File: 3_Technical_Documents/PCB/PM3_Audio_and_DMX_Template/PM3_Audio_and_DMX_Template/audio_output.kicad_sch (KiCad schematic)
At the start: 34 parts, among them U12 OPA2134

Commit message: new push
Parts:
- removed C52: 2.2nF COG, Capacitor_SMD:C_0603_1608Metric, symbol Device:C
- removed C61: 22u, Capacitor_SMD:CP_Elec_6.3x7.7, symbol Device:C_Polarized
- removed R65: 4.99k, Resistor_SMD:R_0603_1608Metric, symbol Device:R
- renumbered C50 to C66, C57 to C67, C54 to C68, C58 to C69, C55 to C71, C59 to C72, C56 to C73, C60 to C74, C47 to C75, C51 to C76, C62 to C77, C49 to C78, C53 to C79, C72 to C80, R24 to R46, R37 to R47, R39 to R48, R40 to R49, R38 to R50, R41 to R51, R31 to R52, R36 to R53, R42 to R54, R43 to R55, R32 to R56, R44 to R57, R34 to R58, R45 to R59, R35 to R60, R46 to R61, U12 to U14
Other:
- note added: "Analog Output"

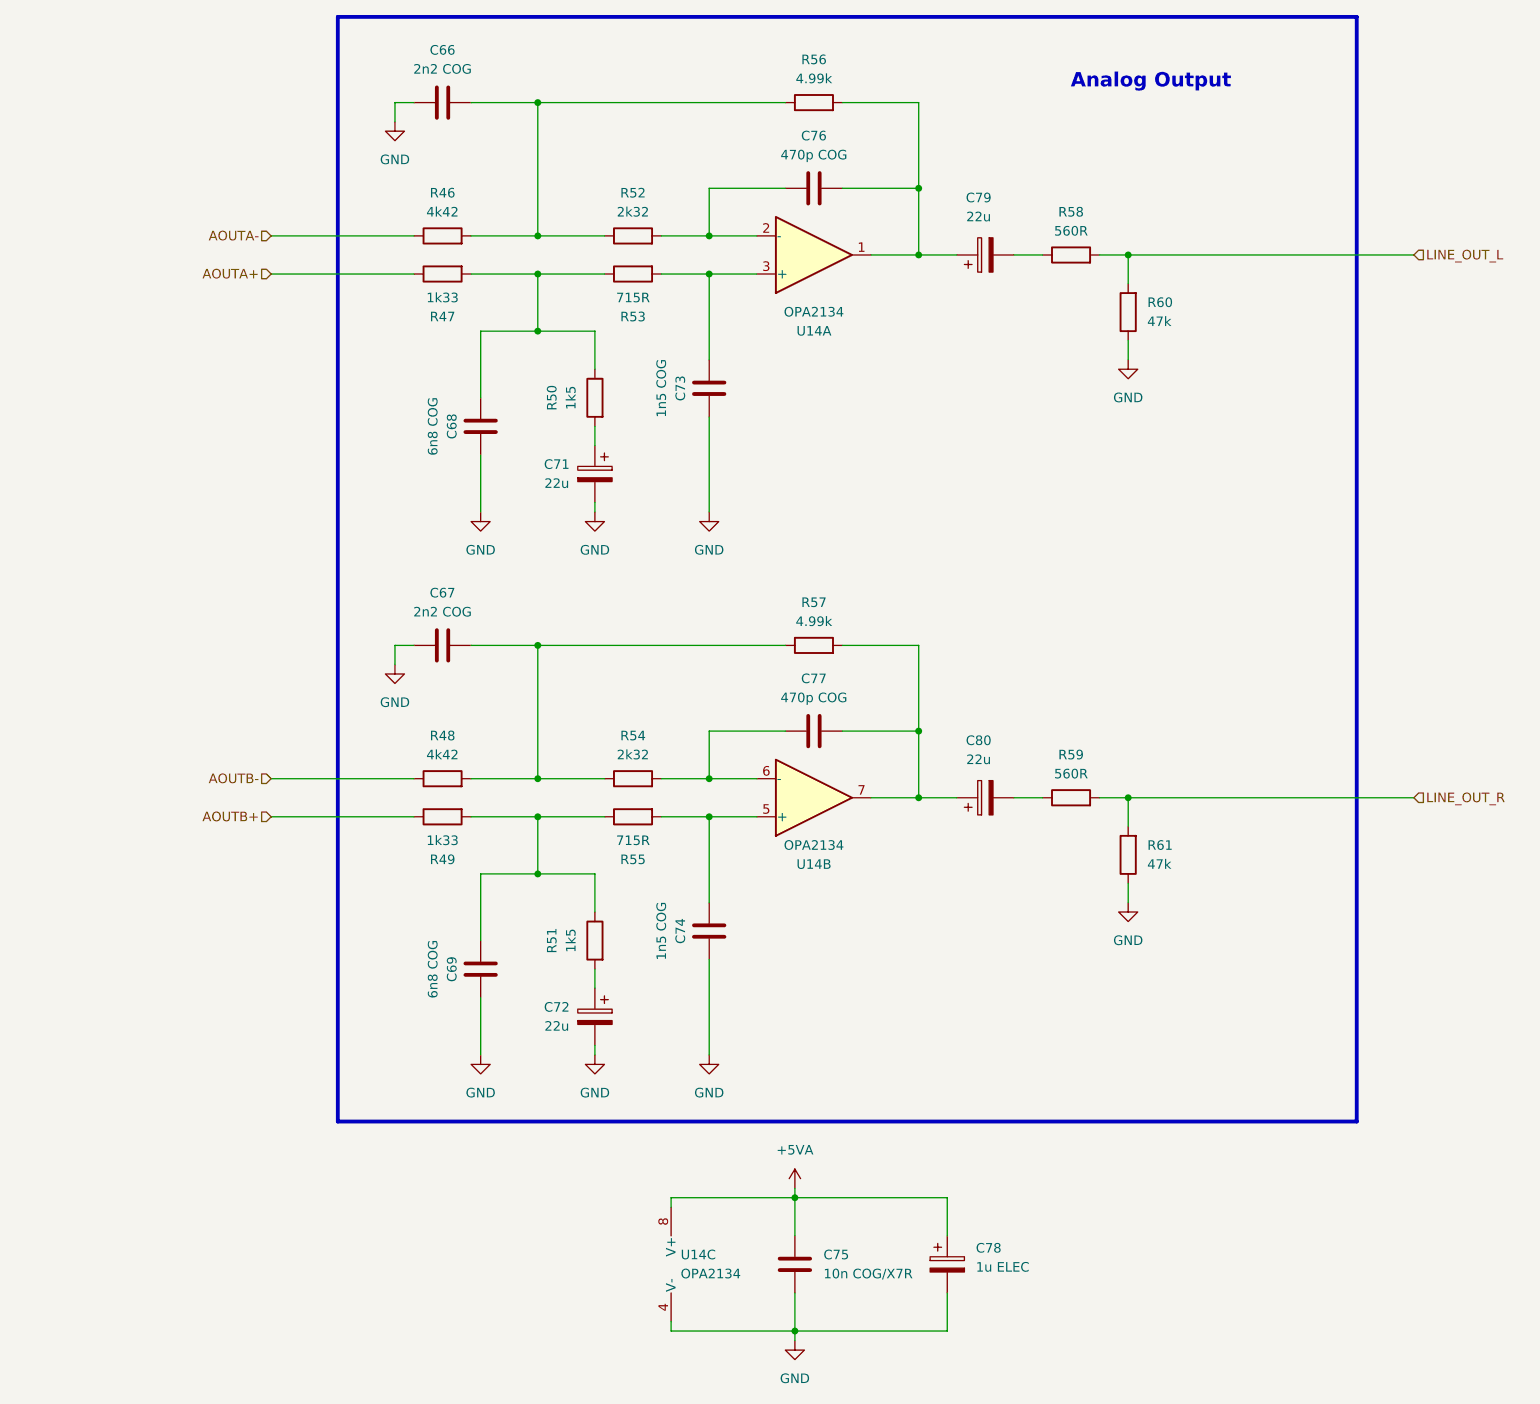
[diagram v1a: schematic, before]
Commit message: rework esp32, codec and layout
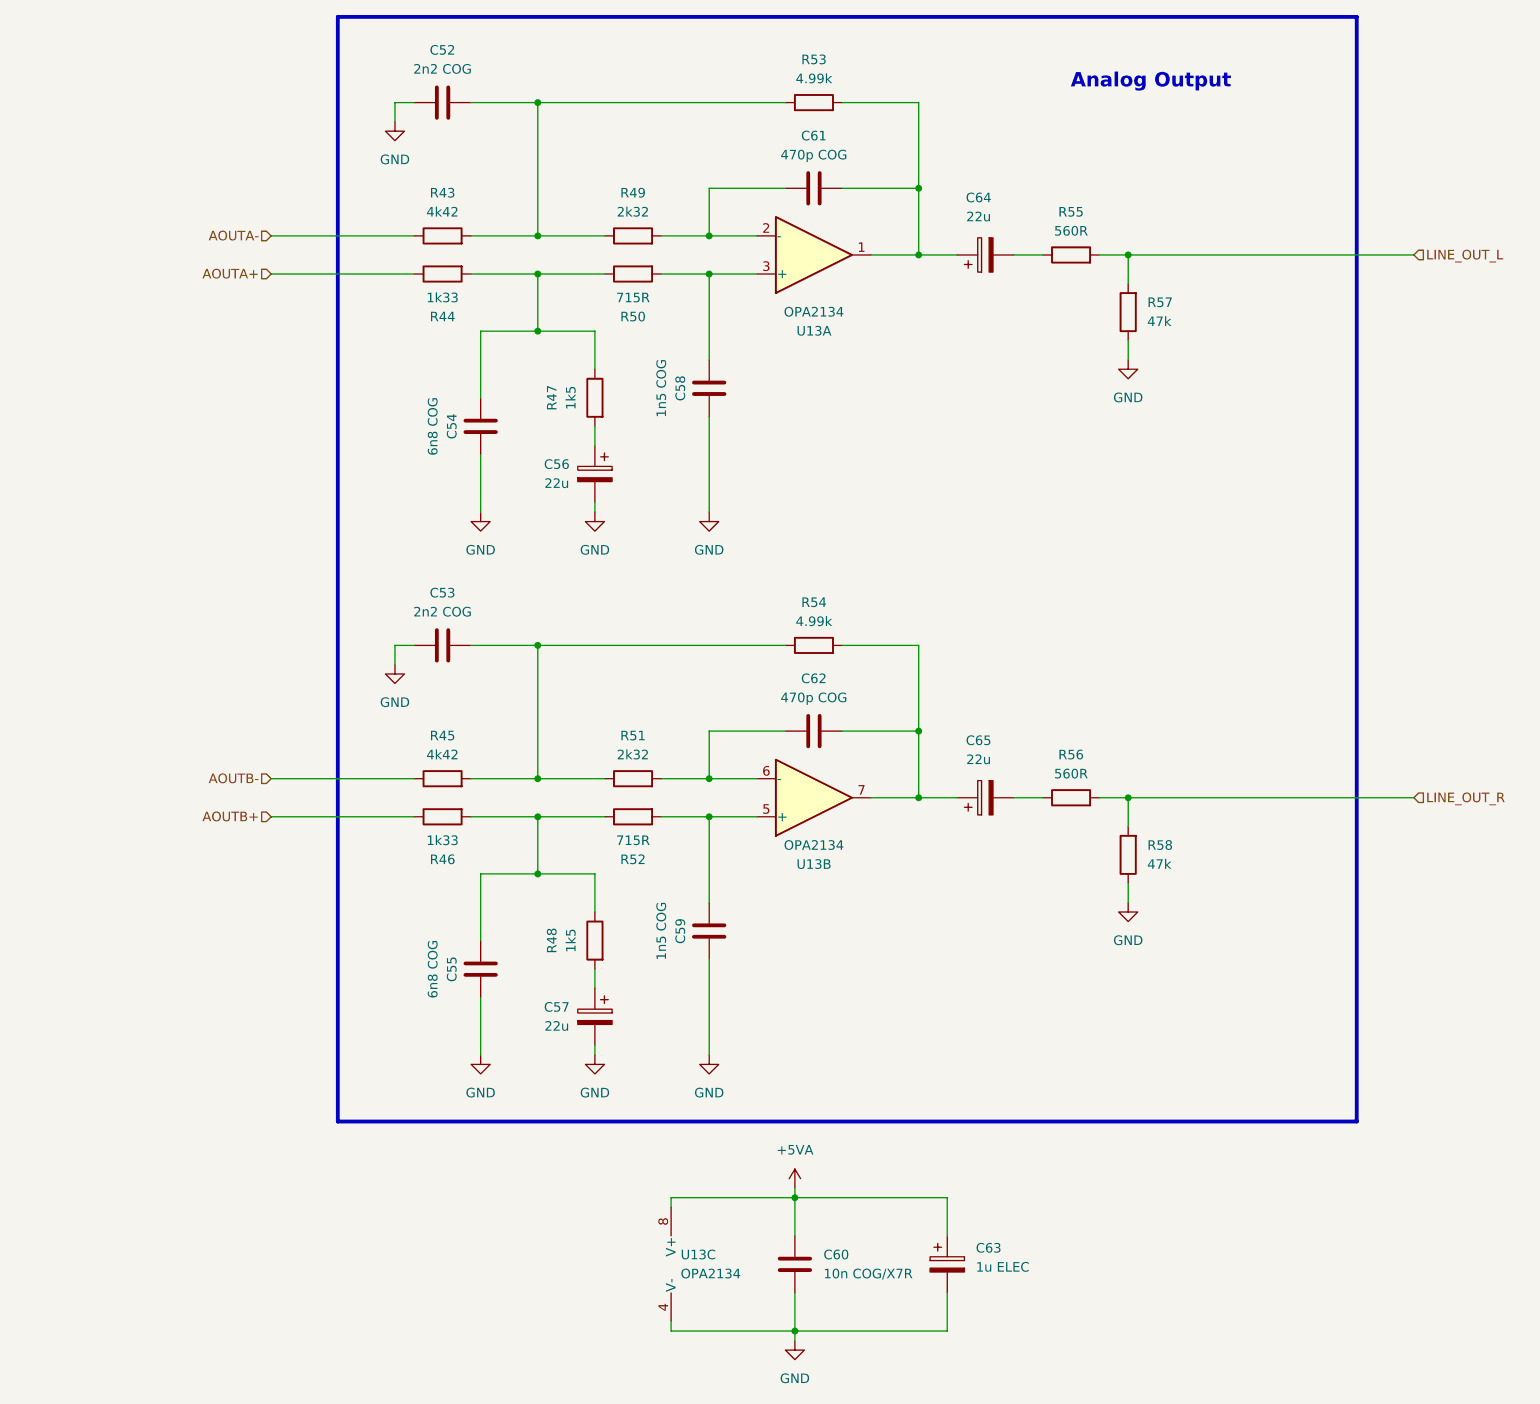
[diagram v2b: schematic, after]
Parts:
- renumbered C66 to C52, C67 to C53, C68 to C54, C69 to C55, C71 to C56, C72 to C57, C73 to C58, C74 to C59, C75 to C60, C76 to C61, C77 to C62, C78 to C63, C79 to C64, C80 to C65, R46 to R43, R47 to R44, R48 to R45, R49 to R46, R50 to R47, R51 to R48, R52 to R49, R53 to R50, R54 to R51, R55 to R52, R56 to R53, R57 to R54, R58 to R55, R59 to R56, R60 to R57, R61 to R58, U14 to U13

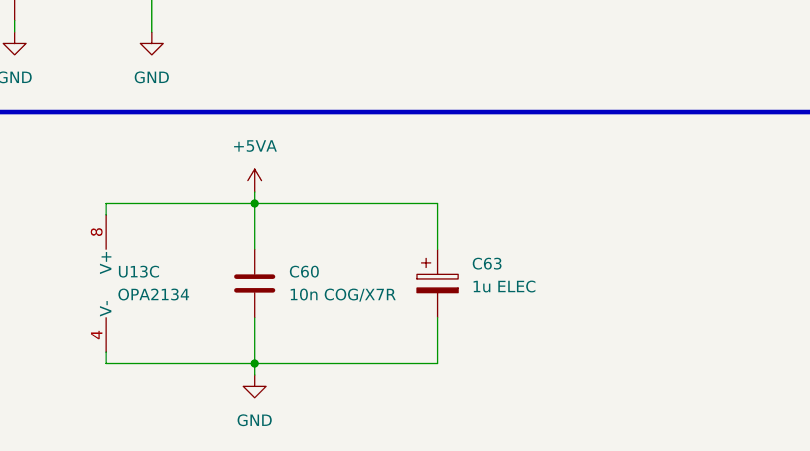
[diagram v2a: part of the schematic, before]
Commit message: updated capacitors
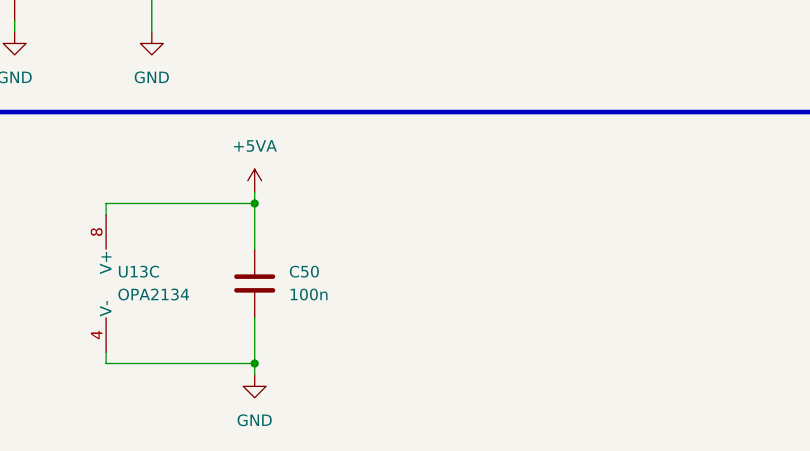
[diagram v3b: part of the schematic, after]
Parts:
- removed C60: 10n COG/X7R, Capacitor_SMD:C_0603_1608Metric, symbol Device:C
- removed C63: 1u ELEC, Capacitor_SMD:CP_Elec_4x5.8, symbol Device:C_Polarized
- added C50: 100n, Capacitor_SMD:C_0603_1608Metric, symbol Device:C
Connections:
- net +5VA: now also C50.1
- net GND: now also C50.2
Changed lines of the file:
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@@
 	(wire
 		(pts
-			(xy 143.51 189.23) (xy 163.83 189.23)
-		)
-		(stroke
-			(width 0)
-			(type default)
-		)
-	)
-	(wire
-		(pts
 			(xy 109.22 55.88) (xy 116.84 55.88)
 		)
@@
 	(wire
 		(pts
-			(xy 163.83 176.53) (xy 163.83 171.45)
-		)
-		(stroke
-			(width 0)
-			(type default)
-		)
-	)
-	(wire
-		(pts
 			(xy 127 187.96) (xy 127 189.23)
 		)
@@
 	(wire
 		(pts
-			(xy 163.83 189.23) (xy 163.83 184.15)
-		)
-		(stroke
-			(width 0)
-			(type default)
-		)
-	)
-	(wire
-		(pts
 			(xy 132.08 132.08) (xy 132.08 120.65)
 		)
@@
 	(wire
 		(pts
-			(xy 143.51 171.45) (xy 163.83 171.45)
-		)
-		(stroke
-			(width 0)
-			(type default)
-		)
-	)
-	(wire
-		(pts
 			(xy 109.22 25.4) (xy 142.24 25.4)
 		)
@@
 	)
 	(symbol
-		(lib_id "Device:C_Polarized")
-		(at 163.83 180.34 0)
-		(unit 1)
-		(exclude_from_sim no)
-		(in_bom yes)
-		(on_board yes)
-		(dnp no)
-		(fields_autoplaced yes)
-		(property "Reference" "C63"
-			(at 167.64 178.1809 0)
-			(effects
-				(font
-					(size 1.27 1.27)
-				)
-				(justify left)
-			)
-		)
-		(property "Value" "1u ELEC"
-			(at 167.64 180.7209 0)
-			(effects
-				(font
-					(size 1.27 1.27)
-				)
-				(justify left)
-			)
-		)
-		(property "Footprint" "Capacitor_SMD:CP_Elec_4x5.8"
-			(at 164.7952 184.15 0)
-			(effects
-				(font
-					(size 1.27 1.27)
-				)
-				(hide yes)
-			)
-		)
-		(property "Datasheet" "~"
-			(at 163.83 180.34 0)
-			(effects
-				(font
-					(size 1.27 1.27)
-				)
-				(hide yes)
-			)
-		)
-		(property "Description" "Polarized capacitor"
-			(at 163.83 180.34 0)
-			(effects
-				(font
-					(size 1.27 1.27)
-				)
-				(hide yes)
-			)
-		)
-		(property "MPN" "EEE1HA010SR"
-			(at 163.83 180.34 90)
-			(effects
-				(font
-					(size 1.27 1.27)
-				)
-				(hide yes)
-			)
-		)
-		(property "Manufacturer" "Panasonic"
-			(at 163.83 180.34 90)
-			(effects
-				(font
-					(size 1.27 1.27)
-				)
-				(hide yes)
-			)
-		)
-		(pin "1"
-		)
-		(pin "2"
-		)
-		(instances
-			(project "PM3_Audio_and_DMX"
-				(path "/1f276d59-ad9b-4e70-a842-f3b7e562eb9b/2329d9ea-d5d7-4913-84c5-e85a54af032e/5f71fd42-8f86-4900-bb58-dbcd17a8cc2c/0d1d0148-6c34-461b-860b-63716d190b68"
-					(reference "C63")
-					(unit 1)
-				)
-			)
-		)
-	)
-	(symbol
 		(lib_id "Device:R")
 		(at 96.52 48.26 90)
@@
 	)
 	(symbol
-		(lib_id "Device:C")
-		(at 143.51 180.34 0)
-		(unit 1)
-		(exclude_from_sim no)
-		(in_bom yes)
-		(on_board yes)
-		(dnp no)
-		(fields_autoplaced yes)
-		(property "Reference" "C60"
-			(at 147.32 179.0699 0)
-			(effects
-				(font
-					(size 1.27 1.27)
-				)
-				(justify left)
-			)
-		)
-		(property "Value" "10n COG/X7R"
-			(at 147.32 181.6099 0)
-			(effects
-				(font
-					(size 1.27 1.27)
-				)
-				(justify left)
-			)
-		)
-		(property "Footprint" "Capacitor_SMD:C_0603_1608Metric"
-			(at 144.4752 184.15 0)
-			(effects
-				(font
-					(size 1.27 1.27)
-				)
-				(hide yes)
-			)
-		)
-		(property "Datasheet" "~"
-			(at 143.51 180.34 0)
-			(effects
-				(font
-					(size 1.27 1.27)
-				)
-				(hide yes)
-			)
-		)
-		(property "Description" "Unpolarized capacitor"
-			(at 143.51 180.34 0)
-			(effects
-				(font
-					(size 1.27 1.27)
-				)
-				(hide yes)
-			)
-		)
-		(property "MPN" "GPC0603103"
-			(at 143.51 180.34 0)
-			(effects
-				(font
-					(size 1.27 1.27)
-				)
-				(hide yes)
-			)
-		)
-		(property "Manufacturer" ""
-			(at 143.51 180.34 0)
-			(effects
-				(font
-					(size 1.27 1.27)
-				)
-				(hide yes)
-			)
-		)
-		(pin "1"
-		)
-		(pin "2"
-		)
-		(instances
-			(project "PM3_Audio_and_DMX"
-				(path "/1f276d59-ad9b-4e70-a842-f3b7e562eb9b/2329d9ea-d5d7-4913-84c5-e85a54af032e/5f71fd42-8f86-4900-bb58-dbcd17a8cc2c/0d1d0148-6c34-461b-860b-63716d190b68"
-					(reference "C60")
-					(unit 1)
-				)
-			)
-		)
-	)
-	(symbol
 		(lib_name "GND_1")
 		(lib_id "power:GND")
@@
 					(unit 1)
 				)
+			)
+		)
+	)
+	(symbol
+		(lib_id "Device:C")
+		(at 143.51 180.34 0)
+		(unit 1)
+		(exclude_from_sim no)
+		(in_bom yes)
+		(on_board yes)
+		(dnp no)
+		(fields_autoplaced yes)
+		(property "Reference" "C50"
+			(at 147.32 179.0699 0)
+			(effects
+				(font
+					(size 1.27 1.27)
+				)
+				(justify left)
+			)
+		)
+		(property "Value" "100n"
+			(at 147.32 181.6099 0)
+			(effects
+				(font
+					(size 1.27 1.27)
+				)
+				(justify left)
+			)
+		)
+		(property "Footprint" "Capacitor_SMD:C_0603_1608Metric"
+			(at 144.4752 184.15 0)
+			(effects
+				(font
+					(size 1.27 1.27)
+				)
+				(hide yes)
+			)
+		)
+		(property "Datasheet" "~"
+			(at 143.51 180.34 0)
+			(effects
+				(font
+					(size 1.27 1.27)
+				)
+				(hide yes)
+			)
+		)
+		(property "Description" "Unpolarized capacitor"
+			(at 143.51 180.34 0)
+			(effects
+				(font
+					(size 1.27 1.27)
+				)
+				(hide yes)
+			)
+		)
+		(property "MPN" "GPC0603104-X7R"
+			(at 143.51 180.34 0)
+			(effects
+				(font
+					(size 1.27 1.27)
+				)
+				(hide yes)
+			)
+		)
+		(property "Manufacturer" ""
+			(at 143.51 180.34 0)
+			(effects
+				(font
+					(size 1.27 1.27)
+				)
+				(hide yes)
+			)
+		)
+		(pin "1"
+		)
+		(pin "2"
+		)
+		(instances
+			(project "PM3_Audio_and_DMX"
+				(path "/1f276d59-ad9b-4e70-a842-f3b7e562eb9b/2329d9ea-d5d7-4913-84c5-e85a54af032e/5f71fd42-8f86-4900-bb58-dbcd17a8cc2c/0d1d0148-6c34-461b-860b-63716d190b68"
+					(reference "C50")
+					(unit 1)
+				)

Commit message: esp-stm connection (+ conflict recolution)
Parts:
- removed C50: 100n, Capacitor_SMD:C_0603_1608Metric, symbol Device:C
- added C60: 100n, Capacitor_SMD:C_0603_1608Metric, symbol Device:C
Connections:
- net +5VA: now also C60.1
- net GND: now also C60.2
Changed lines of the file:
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@@
+	)
+	(symbol
+		(lib_id "Device:C")
+		(at 143.51 180.34 0)
+		(unit 1)
+		(exclude_from_sim no)
+		(in_bom yes)
+		(on_board yes)
+		(dnp no)
+		(fields_autoplaced yes)
+		(property "Reference" "C60"
+			(at 147.32 179.0699 0)
+			(effects
+				(font
+					(size 1.27 1.27)
+				)
+				(justify left)
+			)
+		)
+		(property "Value" "100n"
+			(at 147.32 181.6099 0)
+			(effects
+				(font
+					(size 1.27 1.27)
+				)
+				(justify left)
+			)
+		)
+		(property "Footprint" "Capacitor_SMD:C_0603_1608Metric"
+			(at 144.4752 184.15 0)
+			(effects
+				(font
+					(size 1.27 1.27)
+				)
+				(hide yes)
+			)
+		)
+		(property "Datasheet" "~"
+			(at 143.51 180.34 0)
+			(effects
+				(font
+					(size 1.27 1.27)
+				)
+				(hide yes)
+			)
+		)
+		(property "Description" "Unpolarized capacitor"
+			(at 143.51 180.34 0)
+			(effects
+				(font
+					(size 1.27 1.27)
+				)
+				(hide yes)
+			)
+		)
+		(property "MPN" "GPC0603104-X7R"
+			(at 143.51 180.34 0)
+			(effects
+				(font
+					(size 1.27 1.27)
+				)
+				(hide yes)
+			)
+		)
+		(property "Manufacturer" ""
+			(at 143.51 180.34 0)
+			(effects
+				(font
+					(size 1.27 1.27)
+				)
+				(hide yes)
+			)
+		)
+		(pin "2"
+		)
+		(pin "1"
+		)
+		(instances
+			(project "PM3_Audio_and_DMX"
+				(path "/1f276d59-ad9b-4e70-a842-f3b7e562eb9b/2329d9ea-d5d7-4913-84c5-e85a54af032e/5f71fd42-8f86-4900-bb58-dbcd17a8cc2c/0d1d0148-6c34-461b-860b-63716d190b68"
+					(reference "C60")
+					(unit 1)
+				)
+			)
+		)
 	)
 	(symbol
@@
 					(unit 1)
 				)
-			)
-		)
-	)
-	(symbol
-		(lib_id "Device:C")
-		(at 143.51 180.34 0)
-		(unit 1)
-		(exclude_from_sim no)
-		(in_bom yes)
-		(on_board yes)
-		(dnp no)
-		(fields_autoplaced yes)
-		(property "Reference" "C50"
-			(at 147.32 179.0699 0)
-			(effects
-				(font
-					(size 1.27 1.27)
-				)
-				(justify left)
-			)
-		)
-		(property "Value" "100n"
-			(at 147.32 181.6099 0)
-			(effects
-				(font
-					(size 1.27 1.27)
-				)
-				(justify left)
-			)
-		)
-		(property "Footprint" "Capacitor_SMD:C_0603_1608Metric"
-			(at 144.4752 184.15 0)
-			(effects
-				(font
-					(size 1.27 1.27)
-				)
-				(hide yes)
-			)
-		)
-		(property "Datasheet" "~"
-			(at 143.51 180.34 0)
-			(effects
-				(font
-					(size 1.27 1.27)
-				)
-				(hide yes)
-			)
-		)
-		(property "Description" "Unpolarized capacitor"
-			(at 143.51 180.34 0)
-			(effects
-				(font
-					(size 1.27 1.27)
-				)
-				(hide yes)
-			)
-		)
-		(property "MPN" "GPC0603104-X7R"
-			(at 143.51 180.34 0)
-			(effects
-				(font
-					(size 1.27 1.27)
-				)
-				(hide yes)
-			)
-		)
-		(property "Manufacturer" ""
-			(at 143.51 180.34 0)
-			(effects
-				(font
-					(size 1.27 1.27)
-				)
-				(hide yes)
-			)
-		)
-		(pin "1"
-		)
-		(pin "2"
-		)
-		(instances
-			(project "PM3_Audio_and_DMX"
-				(path "/1f276d59-ad9b-4e70-a842-f3b7e562eb9b/2329d9ea-d5d7-4913-84c5-e85a54af032e/5f71fd42-8f86-4900-bb58-dbcd17a8cc2c/0d1d0148-6c34-461b-860b-63716d190b68"
-					(reference "C50")
-					(unit 1)
-				)
